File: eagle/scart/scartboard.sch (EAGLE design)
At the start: 46 parts, among them IC1 25LC080SN, Q1 BC548-TO92-E1-REV, Q2 BC548, Q3 BC548-TO92-E1-REV, Q4 BC548-TO92-E1-REV, T1 BSS138, T3 BSS138, X1 SCART-F

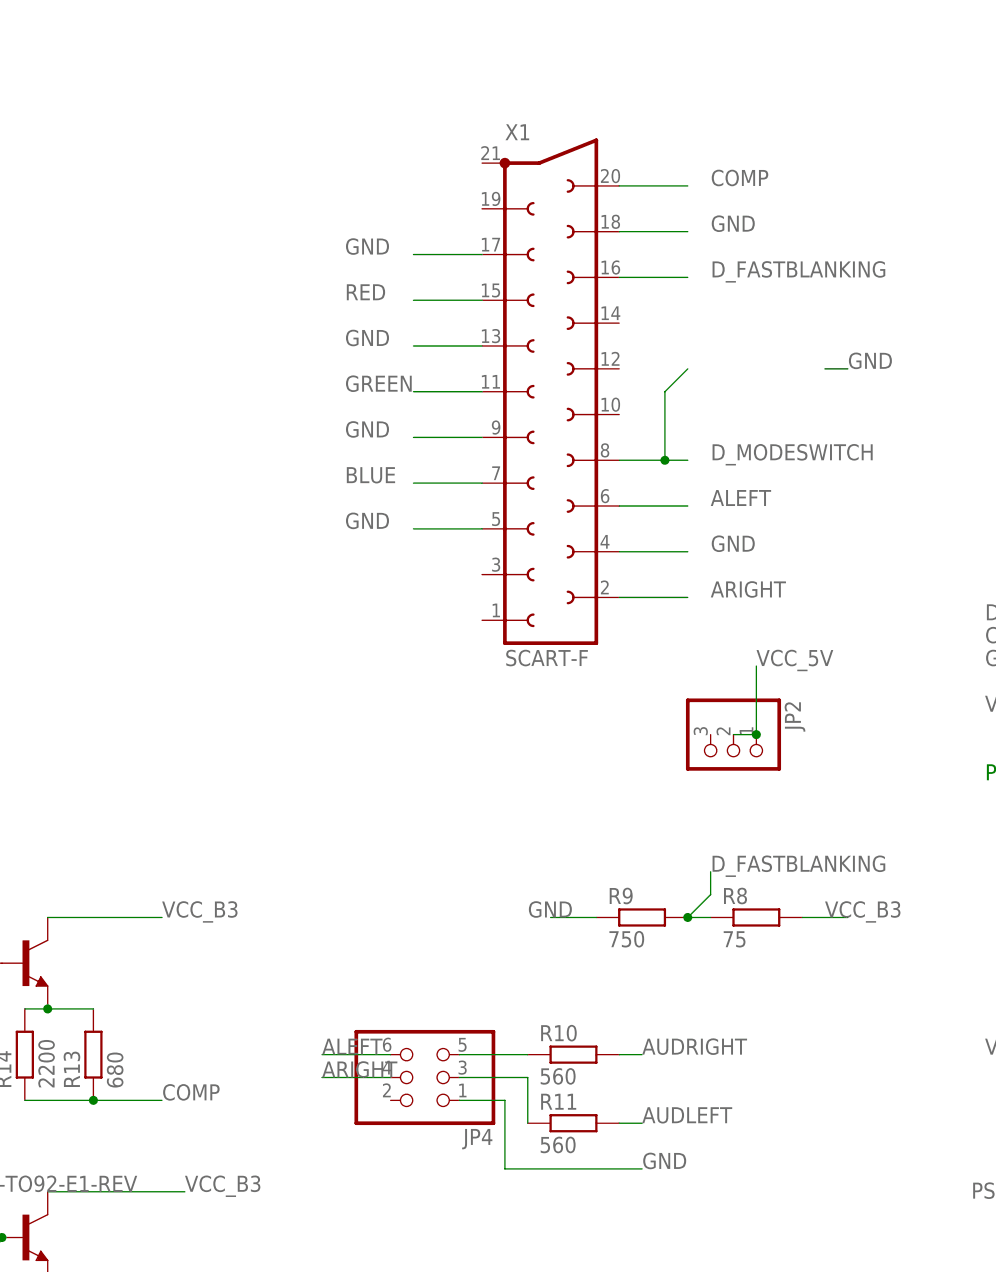
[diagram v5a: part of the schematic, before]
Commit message: fixed scart connector on schematic
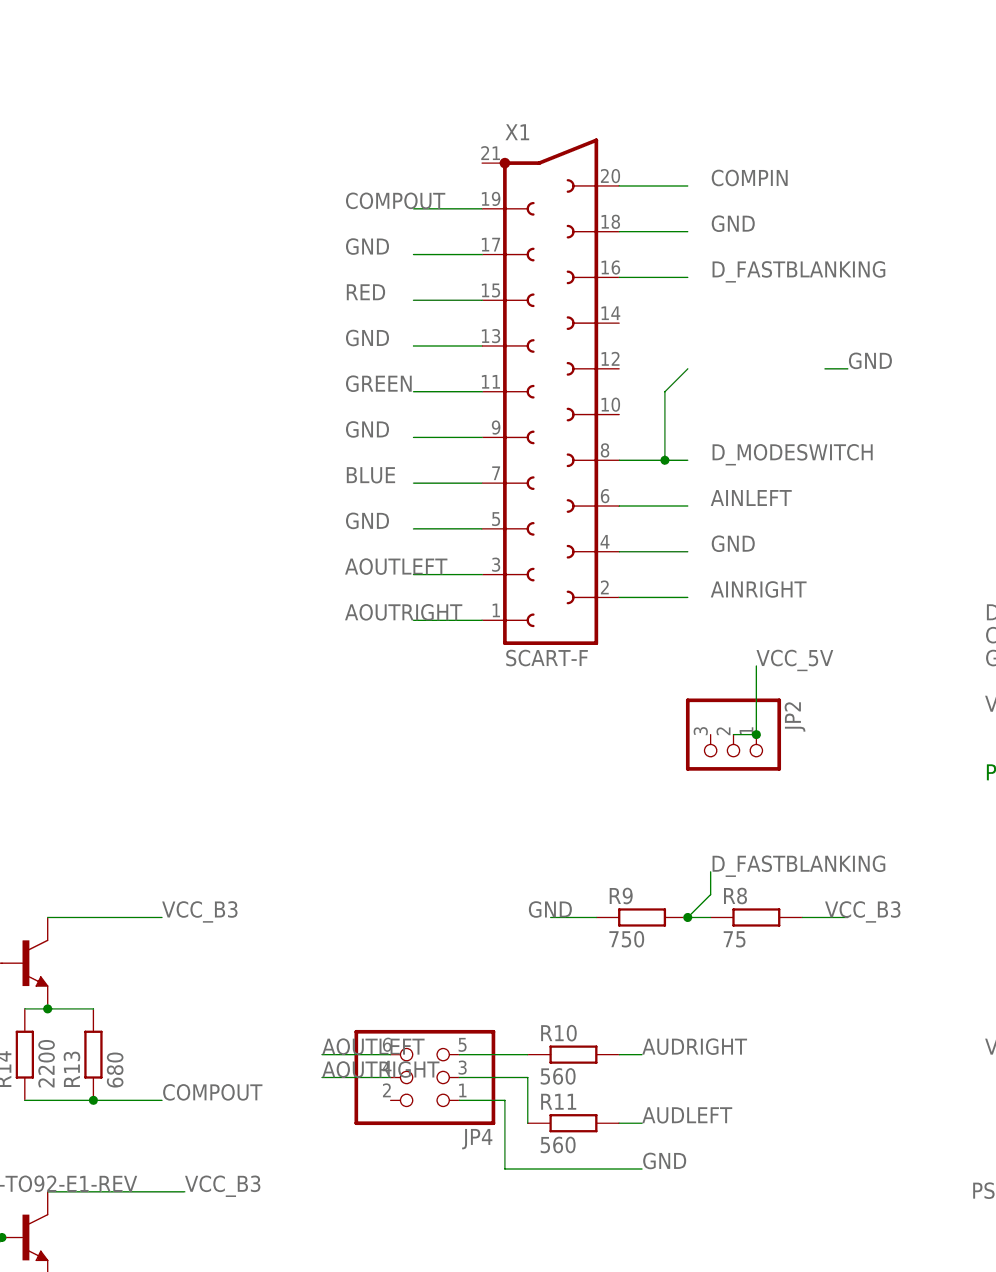
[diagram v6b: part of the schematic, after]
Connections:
- removed net ALEFT: JP4.6, X1.6
- removed net ARIGHT: JP4.4, X1.2
- removed net COMP: R13.1, R14.1, X1.20
- new net AINLEFT: X1.6
- new net AINRIGHT: X1.2
- new net AOUTLEFT: JP4.6, X1.3
- new net AOUTRIGHT: JP4.4, X1.1
- new net COMPIN: X1.20
- new net COMPOUT: R13.1, R14.1, X1.19
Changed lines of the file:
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@@
 </busses>
 <nets>
-<net name="ARIGHT" class="0">
-<segment>
-<pinref part="X1" gate="G$1" pin="2"/>
-<wire x1="45.72" y1="20.32" x2="53.34" y2="20.32" width="0.1524" layer="91"/>
-<label x="55.88" y="20.32" size="1.778" layer="95"/>
-</segment>
-<segment>
-<pinref part="JP4" gate="A" pin="4"/>
-<wire x1="12.7" y1="-33.02" x2="20.32" y2="-33.02" width="0.1524" layer="91"/>
-<label x="12.7" y="-33.02" size="1.778" layer="95"/>
-</segment>
-</net>
-<net name="ALEFT" class="0">
-<segment>
-<pinref part="X1" gate="G$1" pin="6"/>
-<wire x1="45.72" y1="30.48" x2="53.34" y2="30.48" width="0.1524" layer="91"/>
-<label x="55.88" y="30.48" size="1.778" layer="95"/>
-</segment>
+<net name="AOUTLEFT" class="0">
 <segment>
 <pinref part="JP4" gate="A" pin="6"/>
 <wire x1="20.32" y1="-30.48" x2="12.7" y2="-30.48" width="0.1524" layer="91"/>
 <label x="12.7" y="-30.48" size="1.778" layer="95"/>
+</segment>
+<segment>
+<pinref part="X1" gate="G$1" pin="3"/>
+<wire x1="22.86" y1="22.86" x2="30.48" y2="22.86" width="0.1524" layer="91"/>
+<label x="15.24" y="22.86" size="1.778" layer="95"/>
 </segment>
 </net>
@@
 <junction x="53.34" y="-15.24"/>
 <label x="55.88" y="-10.16" size="1.778" layer="95"/>
-</segment>
-</net>
-<net name="COMP" class="0">
-<segment>
-<pinref part="X1" gate="G$1" pin="20"/>
-<wire x1="45.72" y1="66.04" x2="53.34" y2="66.04" width="0.1524" layer="91"/>
-<label x="55.88" y="66.04" size="1.778" layer="95"/>
-</segment>
-<segment>
-<pinref part="R13" gate="G$1" pin="1"/>
-<wire x1="-12.7" y1="-35.56" x2="-5.08" y2="-35.56" width="0.1524" layer="91"/>
-<label x="-5.08" y="-35.56" size="1.778" layer="95"/>
-<pinref part="R14" gate="G$1" pin="1"/>
-<wire x1="-20.32" y1="-35.56" x2="-12.7" y2="-35.56" width="0.1524" layer="91"/>
-<junction x="-12.7" y="-35.56"/>
 </segment>
 </net>
@@
 </segment>
 </net>
+<net name="AOUTRIGHT" class="0">
+<segment>
+<pinref part="X1" gate="G$1" pin="1"/>
+<wire x1="22.86" y1="17.78" x2="30.48" y2="17.78" width="0.1524" layer="91"/>
+<label x="15.24" y="17.78" size="1.778" layer="95"/>
+</segment>
+<segment>
+<pinref part="JP4" gate="A" pin="4"/>
+<wire x1="12.7" y1="-33.02" x2="20.32" y2="-33.02" width="0.1524" layer="91"/>
+<label x="12.7" y="-33.02" size="1.778" layer="95"/>
+</segment>
+</net>
+<net name="COMPOUT" class="0">
+<segment>
+<pinref part="X1" gate="G$1" pin="19"/>
+<wire x1="22.86" y1="63.5" x2="30.48" y2="63.5" width="0.1524" layer="91"/>
+<label x="15.24" y="63.5" size="1.778" layer="95"/>
+</segment>
+<segment>
+<pinref part="R13" gate="G$1" pin="1"/>
+<wire x1="-12.7" y1="-35.56" x2="-5.08" y2="-35.56" width="0.1524" layer="91"/>
+<label x="-5.08" y="-35.56" size="1.778" layer="95"/>
+<pinref part="R14" gate="G$1" pin="1"/>
+<wire x1="-20.32" y1="-35.56" x2="-12.7" y2="-35.56" width="0.1524" layer="91"/>
+<junction x="-12.7" y="-35.56"/>
+</segment>
+</net>
+<net name="AINLEFT" class="0">
+<segment>
+<pinref part="X1" gate="G$1" pin="6"/>
+<wire x1="45.72" y1="30.48" x2="53.34" y2="30.48" width="0.1524" layer="91"/>
+<label x="55.88" y="30.48" size="1.778" layer="95"/>
+</segment>
+</net>
+<net name="AINRIGHT" class="0">
+<segment>
+<pinref part="X1" gate="G$1" pin="2"/>
+<wire x1="45.72" y1="20.32" x2="53.34" y2="20.32" width="0.1524" layer="91"/>
+<label x="55.88" y="20.32" size="1.778" layer="95"/>
+</segment>
+</net>
+<net name="COMPIN" class="0">
+<segment>
+<pinref part="X1" gate="G$1" pin="20"/>
+<wire x1="45.72" y1="66.04" x2="53.34" y2="66.04" width="0.1524" layer="91"/>
+<label x="55.88" y="66.04" size="1.778" layer="95"/>
+</segment>
+</net>

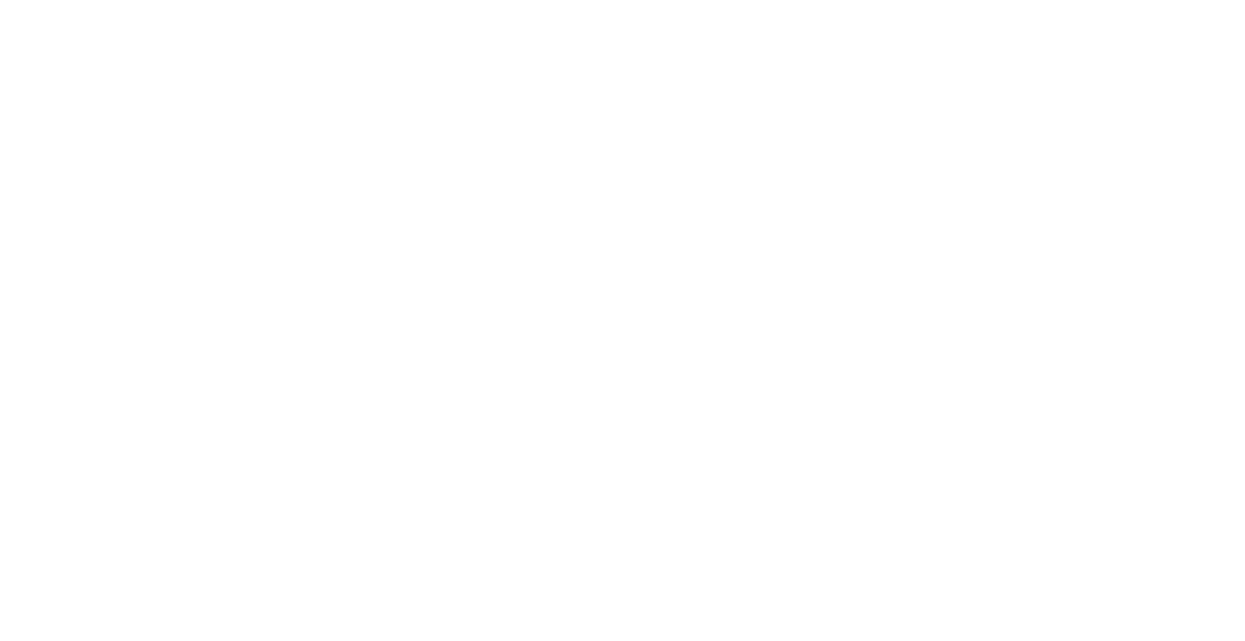
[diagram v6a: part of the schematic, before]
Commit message: added tape in prototype to scartboard
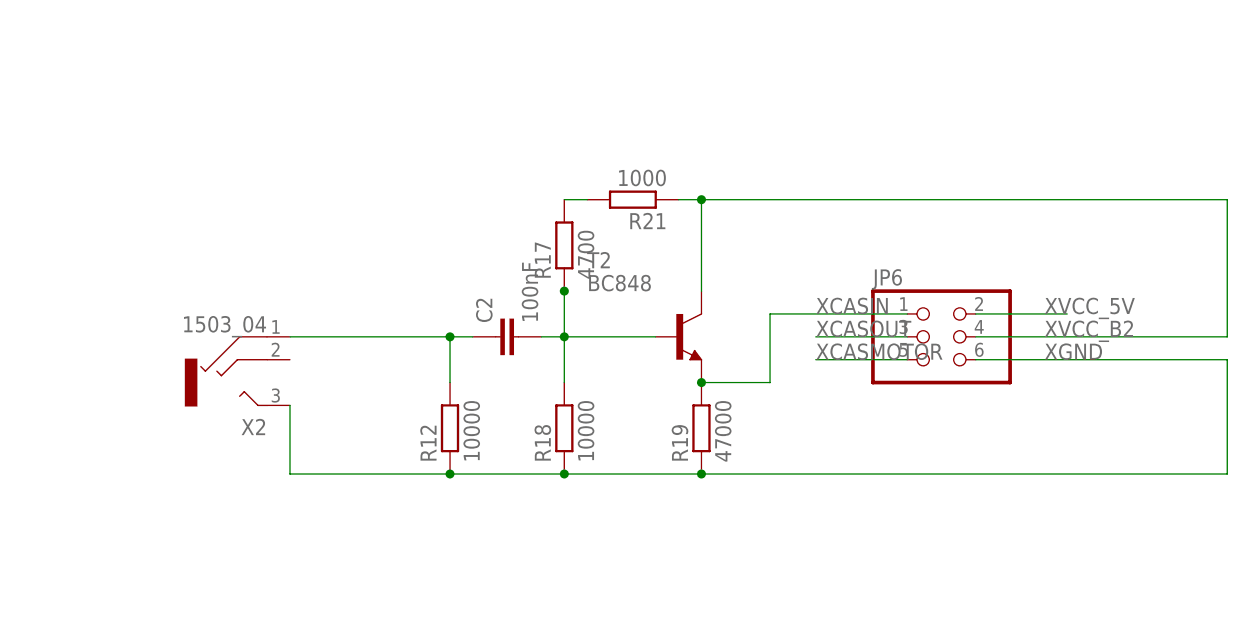
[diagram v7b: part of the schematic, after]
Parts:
- added C2: 100nF, resistor:C-EUC0603
- added JP6: (no value), pinhead:PINHD-2X3
- added R12, R18: 10000, rcl:R-EU_R0805
- added R17: 4700, rcl:R-EU_R0805
- added R19: 47000, rcl:R-EU_R0805
- added R21: 1000, rcl:R-EU_R0805
- added T2: BC848, transistor:BC848
- added X2: 1503_04, con-lumberg:1503_04
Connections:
- new net N$13: R17.2, R21.2
- new net N$14: C2.1, R12.2, X2.1
- new net N$8: C2.2, R17.1, R18.2, T2.B
- new net XCASIN: JP6.1, R19.2, T2.E
- new net XCASMOTOR: JP6.5
- new net XCASOUT: JP6.3
- new net XGND: JP6.6, R12.1, R18.1, R19.1, X2.2
- new net XVCC_5V: JP6.2
- new net XVCC_B2: JP6.4, R21.1, T2.C
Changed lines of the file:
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@@
 <part name="C1" library="rcl" deviceset="C-EU" device="C0603"/>
 <part name="U$1" library="sram" deviceset="AS6C4008" device=""/>
+<part name="JP6" library="pinhead" deviceset="PINHD-2X3" device=""/>
+<part name="R12" library="rcl" deviceset="R-EU_" device="R0805" value="10000"/>
+<part name="R17" library="rcl" deviceset="R-EU_" device="R0805" value="4700"/>
+<part name="R18" library="rcl" deviceset="R-EU_" device="R0805" value="10000"/>
+<part name="R19" library="rcl" deviceset="R-EU_" device="R0805" value="47000"/>
+<part name="C2" library="resistor" deviceset="C-EU" device="C0603" value="100nF"/>
+<part name="T2" library="transistor" deviceset="BC848" device=""/>
+<part name="X2" library="con-lumberg" deviceset="1503_04" device=""/>
+<part name="R21" library="rcl" deviceset="R-EU_" device="R0805" value="1000"/>
 </parts>
 <sheets>
@@
 <instance part="C1" gate="G$1" x="88.9" y="127" rot="R180"/>
 <instance part="U$1" gate="G$1" x="241.3" y="-10.16"/>
+<instance part="JP6" gate="A" x="383.54" y="50.8"/>
+<instance part="R12" gate="G$1" x="330.2" y="40.64" rot="R90"/>
+<instance part="R17" gate="G$1" x="342.9" y="60.96" rot="R90"/>
+<instance part="R18" gate="G$1" x="342.9" y="40.64" rot="R90"/>
+<instance part="R19" gate="G$1" x="358.14" y="40.64" rot="R90"/>
+<instance part="C2" gate="G$1" x="335.28" y="50.8" rot="R90"/>
+<instance part="T2" gate="G$1" x="355.6" y="50.8"/>
+<instance part="X2" gate="G$1" x="307.34" y="45.72" rot="R180"/>
+<instance part="R21" gate="G$1" x="350.52" y="66.04" rot="R180"/>
 </instances>
 <busses>
@@
 </segment>
 </net>
+<net name="XCASIN" class="0">
+<segment>
+<pinref part="JP6" gate="A" pin="1"/>
+<wire x1="381" y1="53.34" x2="365.76" y2="53.34" width="0.1524" layer="91"/>
+<label x="370.84" y="53.34" size="1.778" layer="95"/>
+<pinref part="T2" gate="G$1" pin="E"/>
+<pinref part="R19" gate="G$1" pin="2"/>
+<wire x1="365.76" y1="45.72" x2="358.14" y2="45.72" width="0.1524" layer="91"/>
+<junction x="358.14" y="45.72"/>
+<wire x1="365.76" y1="53.34" x2="365.76" y2="45.72" width="0.1524" layer="91"/>
+</segment>
+</net>
+<net name="XCASOUT" class="0">
+<segment>
+<pinref part="JP6" gate="A" pin="3"/>
+<wire x1="370.84" y1="50.8" x2="381" y2="50.8" width="0.1524" layer="91"/>
+<label x="370.84" y="50.8" size="1.778" layer="95"/>
+</segment>
+</net>
+<net name="XCASMOTOR" class="0">
+<segment>
+<pinref part="JP6" gate="A" pin="5"/>
+<wire x1="370.84" y1="48.26" x2="381" y2="48.26" width="0.1524" layer="91"/>
+<label x="370.84" y="48.26" size="1.778" layer="95"/>
+</segment>
+</net>
+<net name="XGND" class="0">
+<segment>
+<pinref part="JP6" gate="A" pin="6"/>
+<label x="396.24" y="48.26" size="1.778" layer="95"/>
+<pinref part="R19" gate="G$1" pin="1"/>
+<wire x1="358.14" y1="35.56" x2="416.56" y2="35.56" width="0.1524" layer="91"/>
+<wire x1="416.56" y1="35.56" x2="416.56" y2="48.26" width="0.1524" layer="91"/>
+<wire x1="416.56" y1="48.26" x2="388.62" y2="48.26" width="0.1524" layer="91"/>
+<pinref part="R18" gate="G$1" pin="1"/>
+<wire x1="342.9" y1="35.56" x2="358.14" y2="35.56" width="0.1524" layer="91"/>
+<junction x="358.14" y="35.56"/>
+<pinref part="R12" gate="G$1" pin="1"/>
+<wire x1="312.42" y1="35.56" x2="330.2" y2="35.56" width="0.1524" layer="91"/>
+<wire x1="330.2" y1="35.56" x2="342.9" y2="35.56" width="0.1524" layer="91"/>
+<junction x="330.2" y="35.56"/>
+<junction x="342.9" y="35.56"/>
+<pinref part="X2" gate="G$1" pin="2"/>
+<wire x1="312.42" y1="35.56" x2="312.42" y2="43.18" width="0.1524" layer="91"/>
+</segment>
+</net>
+<net name="XVCC_B2" class="0">
+<segment>
+<pinref part="JP6" gate="A" pin="4"/>
+<label x="396.24" y="50.8" size="1.778" layer="95"/>
+<wire x1="358.14" y1="66.04" x2="416.56" y2="66.04" width="0.1524" layer="91"/>
+<wire x1="416.56" y1="66.04" x2="416.56" y2="50.8" width="0.1524" layer="91"/>
+<wire x1="416.56" y1="50.8" x2="388.62" y2="50.8" width="0.1524" layer="91"/>
+<pinref part="T2" gate="G$1" pin="C"/>
+<wire x1="358.14" y1="55.88" x2="358.14" y2="66.04" width="0.1524" layer="91"/>
+<pinref part="R21" gate="G$1" pin="1"/>
+<wire x1="358.14" y1="66.04" x2="355.6" y2="66.04" width="0.1524" layer="91"/>
+<junction x="358.14" y="66.04"/>
+</segment>
+</net>
+<net name="XVCC_5V" class="0">
+<segment>
+<pinref part="JP6" gate="A" pin="2"/>
+<wire x1="398.78" y1="53.34" x2="388.62" y2="53.34" width="0.1524" layer="91"/>
+<label x="396.24" y="53.34" size="1.778" layer="95"/>
+</segment>
+</net>
+<net name="N$8" class="0">
+<segment>
+<pinref part="R17" gate="G$1" pin="1"/>
+<pinref part="R17" gate="G$1" pin="1"/>
+<pinref part="R18" gate="G$1" pin="2"/>
+<wire x1="342.9" y1="45.72" x2="342.9" y2="50.8" width="0.1524" layer="91"/>
+<junction x="342.9" y="55.88"/>
+<pinref part="C2" gate="G$1" pin="2"/>
+<wire x1="342.9" y1="50.8" x2="342.9" y2="55.88" width="0.1524" layer="91"/>
+<wire x1="340.36" y1="50.8" x2="342.9" y2="50.8" width="0.1524" layer="91"/>
+<junction x="342.9" y="50.8"/>
+<pinref part="T2" gate="G$1" pin="B"/>
+<wire x1="353.06" y1="50.8" x2="342.9" y2="50.8" width="0.1524" layer="91"/>
+</segment>
+</net>
+<net name="N$14" class="0">
+<segment>
+<pinref part="C2" gate="G$1" pin="1"/>
+<wire x1="332.74" y1="50.8" x2="330.2" y2="50.8" width="0.1524" layer="91"/>
+<pinref part="R12" gate="G$1" pin="2"/>
+<wire x1="330.2" y1="50.8" x2="312.42" y2="50.8" width="0.1524" layer="91"/>
+<wire x1="330.2" y1="45.72" x2="330.2" y2="50.8" width="0.1524" layer="91"/>
+<junction x="330.2" y="50.8"/>
+<pinref part="X2" gate="G$1" pin="1"/>
+</segment>
+</net>
+<net name="N$13" class="0">
+<segment>
+<pinref part="R21" gate="G$1" pin="2"/>
+<pinref part="R17" gate="G$1" pin="2"/>
+<wire x1="345.44" y1="66.04" x2="342.9" y2="66.04" width="0.1524" layer="91"/>
+</segment>
+</net>
